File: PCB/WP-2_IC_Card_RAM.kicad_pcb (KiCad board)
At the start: 2 copper layers, 45 x 54 mm, 11 parts, among them J1 Conn_01x38_Female, U1 SRAM 128Kx8 5v Parallel, U2 SRAM 128Kx8 5v Parallel

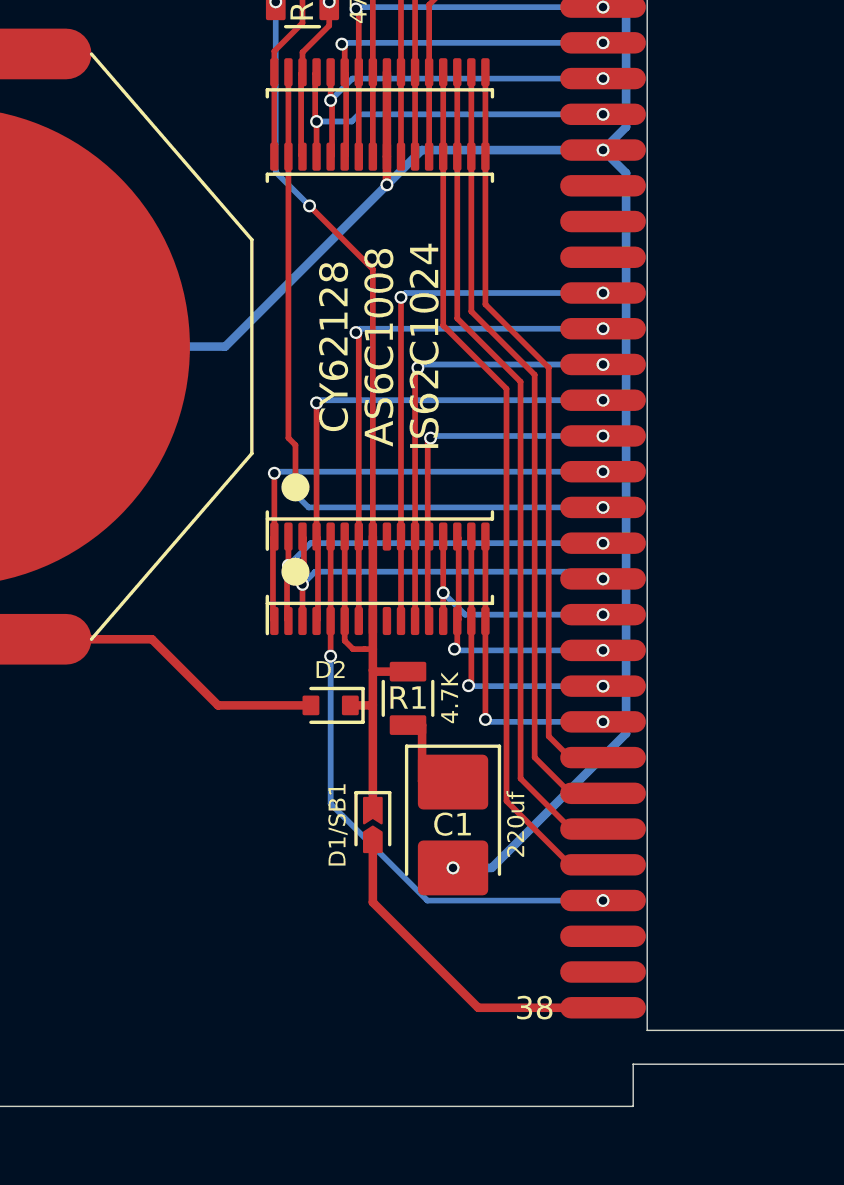
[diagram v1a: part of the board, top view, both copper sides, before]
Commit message: cap & diodes on ram card
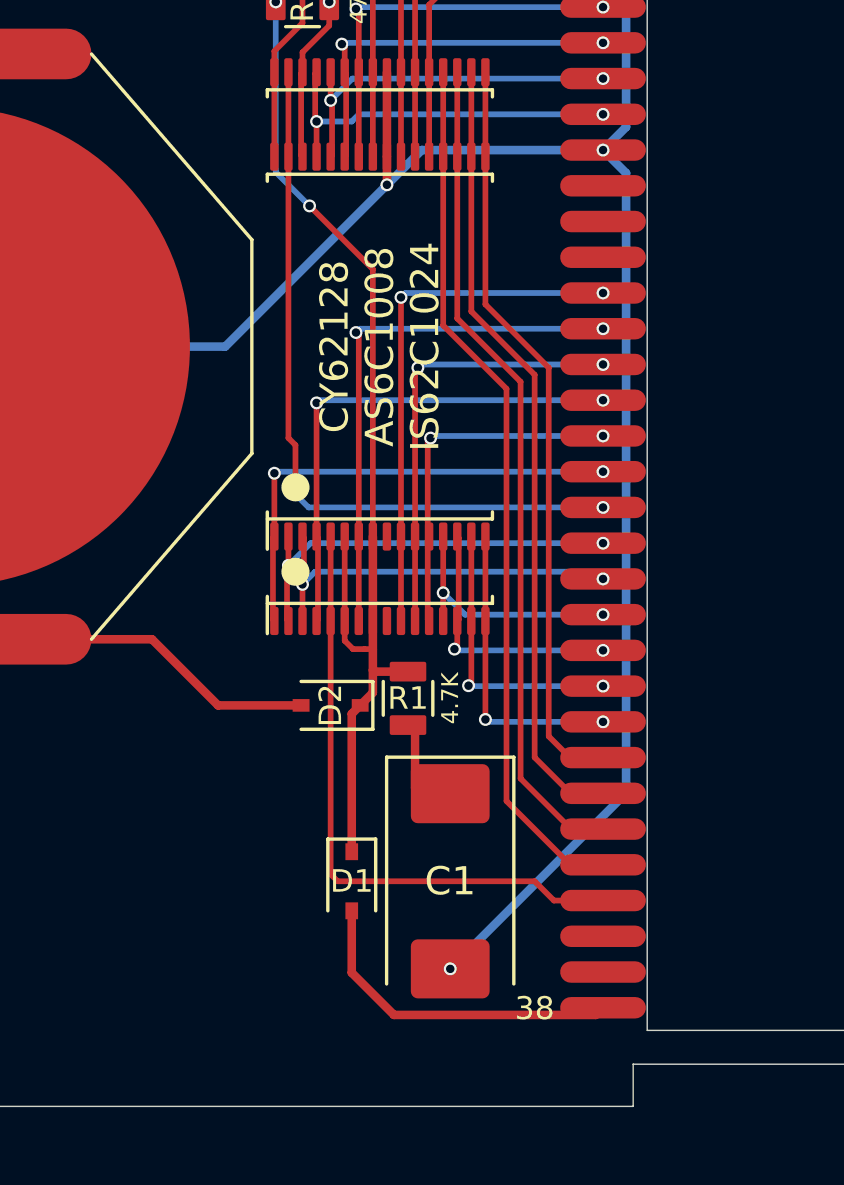
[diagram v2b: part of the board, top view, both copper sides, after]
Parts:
- C1: footprint 0_LOCAL:CP_Tantalum_Case-B_EIA-3528-21_Reflow -> 0_LOCAL:CP_EIA-7343-20_AVX-Y
- D1: renamed from D1/SB1; value 1SS389 -> CUS520,H3F; footprint 0_LOCAL:D_SOD-523_bridgeable -> 0_LOCAL:D_SOD-323
- D2: value 1SS389 -> CUS520,H3F; footprint 0_LOCAL:D_SOD-523 -> 0_LOCAL:D_SOD-323
- moved D1 2.14 mm to (148.2, 118.7)
- moved C1 2.00 mm to (151.8, 118.7)
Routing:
- net GND: track 77.0 -> 79.8 mm
- net /R~W: track 20.6 -> 22.1 mm, vias 2 -> 0
- net VMEM: track 32.3 -> 33.5 mm
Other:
- board text added: "WP-2_IC_Card_RAM_cap_batt_no_carrier v002"
- board text removed: "WP-2_IC_Card_RAM_cap_batt_no_carrier v001"

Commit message: readme
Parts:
- moved D2 0.25 mm to (147.5, 112.2)
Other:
- outline, holes or cut-outs redrawn

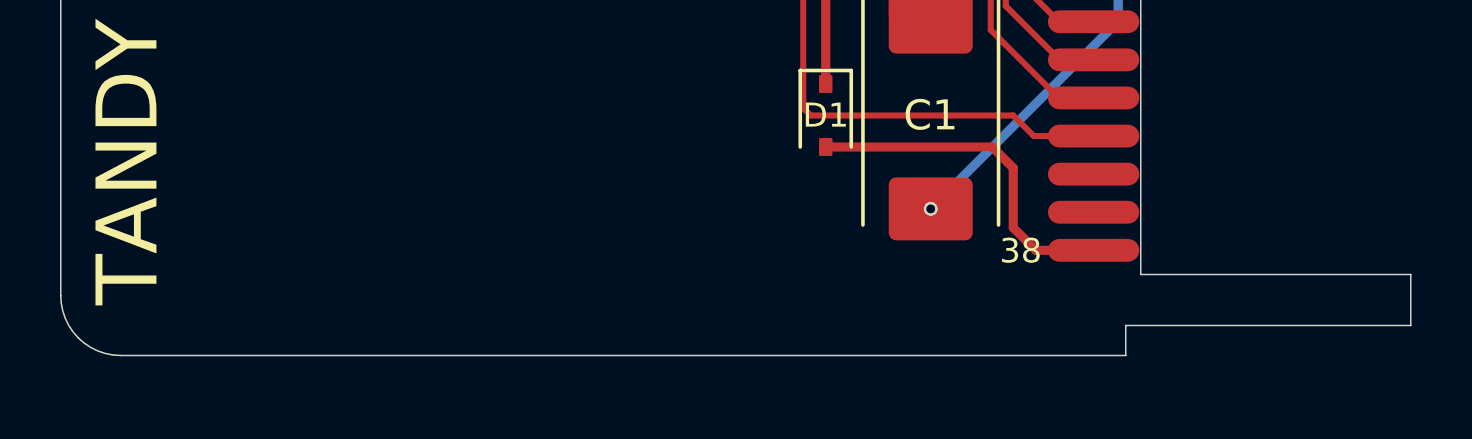
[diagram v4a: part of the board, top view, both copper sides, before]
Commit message: silkscreen board name, small board outline tweak
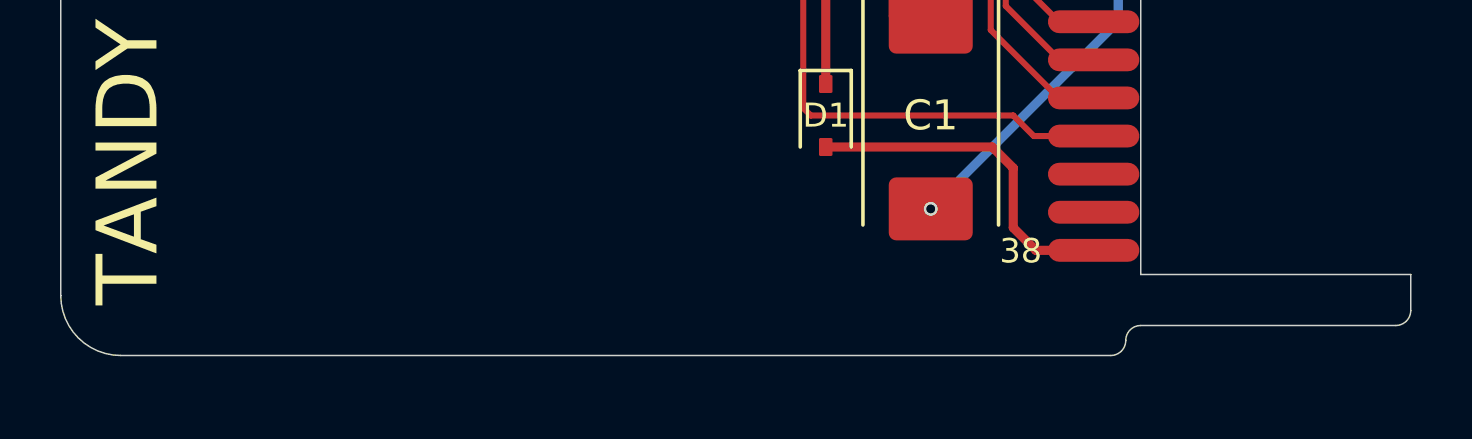
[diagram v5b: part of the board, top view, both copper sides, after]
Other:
- outline, holes or cut-outs redrawn
- board text added: "WP-2_IC_Card_RAM v002"
- board text removed: "WP-2_IC_Card_RAM_cap_batt_no_carrier v002"

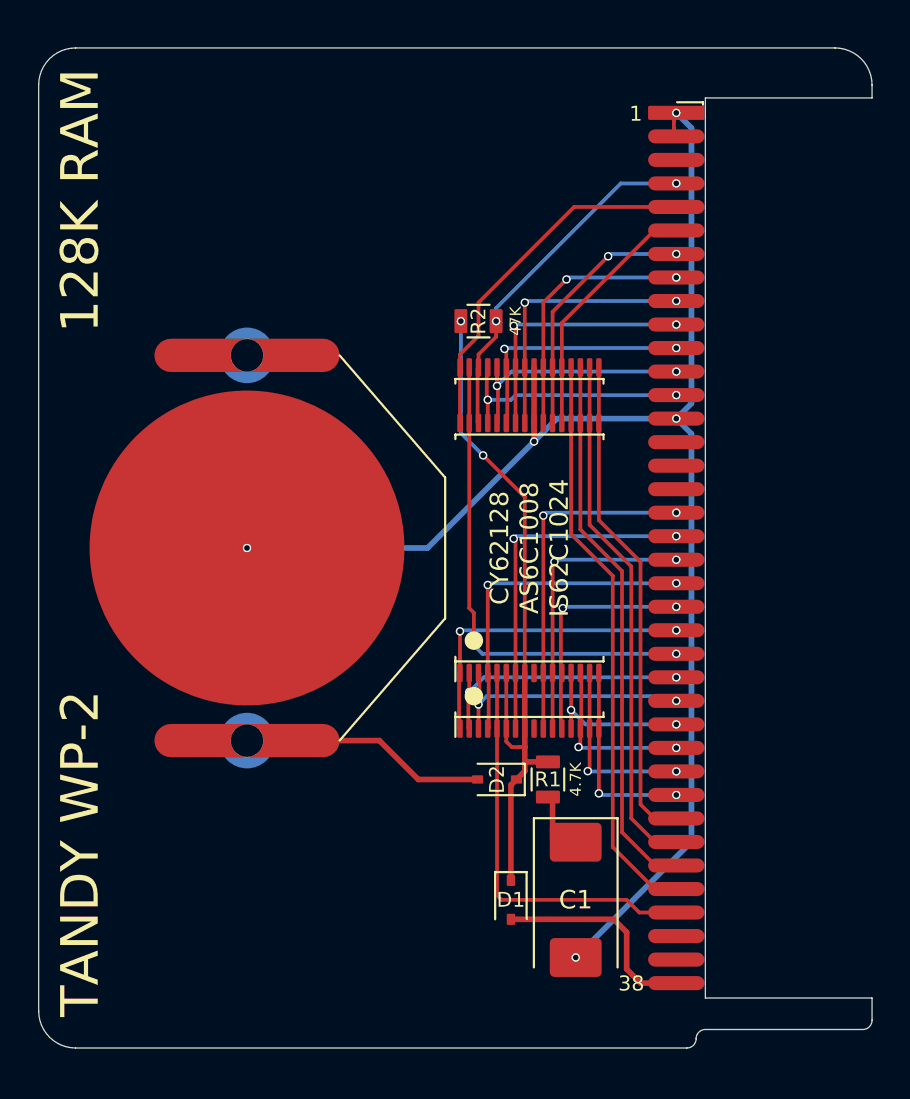
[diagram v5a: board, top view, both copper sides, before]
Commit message: v003 - edge cut finger pulls, easier diodes and batt holder for RAM
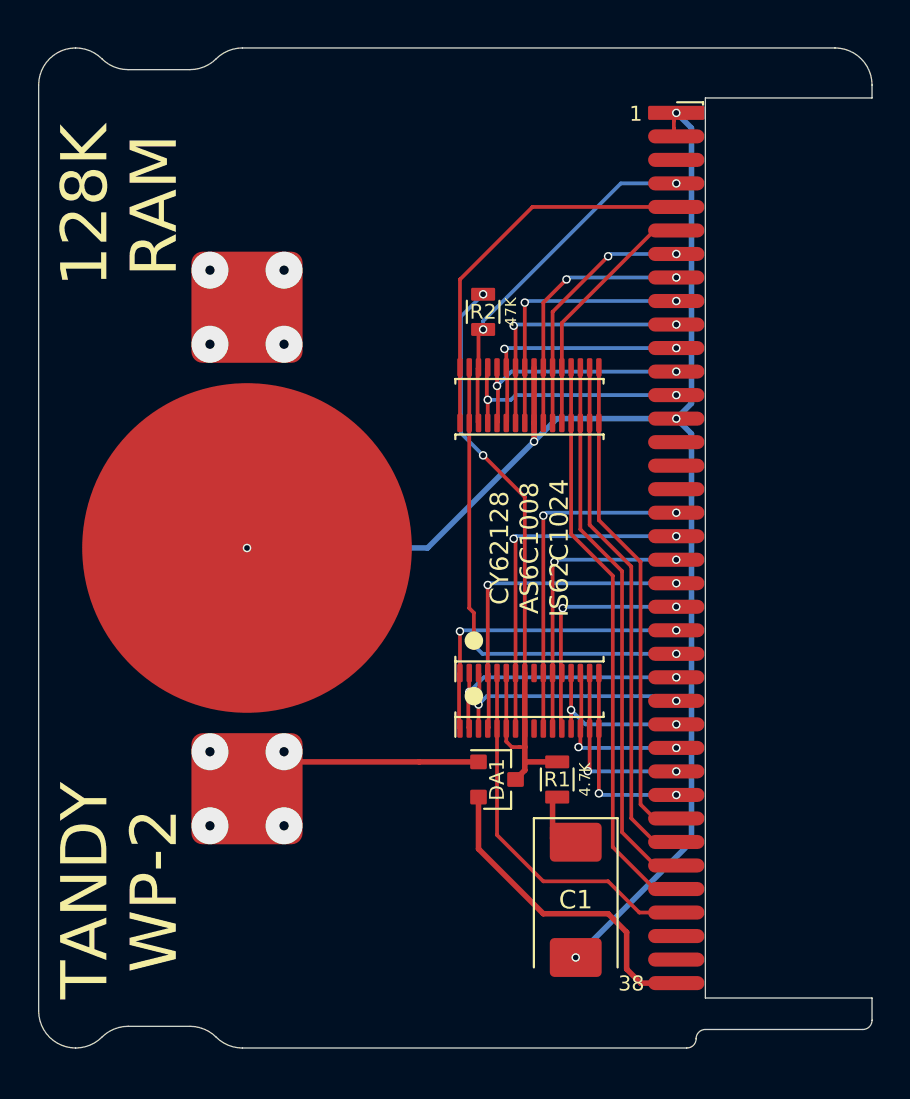
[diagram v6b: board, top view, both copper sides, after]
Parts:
- removed D1, D2: CUS520,H3F, 0_LOCAL:D_SOD-323
- added DA1: BAT54C, 0_LOCAL:SOT-23, F.Cu at (147.5, 112.2)
- BT1: value Battery CR2016 3v -> CR2016 3v; footprint 0_LOCAL:2016_battery_holder_tht -> 0_LOCAL:2016_battery_holder_smt
- moved R2 0.56 mm to (146.8, 86.9), turned to 270 degrees
- moved R1 0.50 mm to (150.8, 112.2)
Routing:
- net VBUS: track 11.5 -> 17.6 mm
- net VMEM: track 33.5 -> 30.4 mm
- net /R~W: track 22.1 -> 20.2 mm
- net /~OE: track 19.7 -> 21.1 mm
- net Net-(BT1-Pad1): track 13.3 -> 13.1 mm, vias 0 -> 8
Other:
- outline, holes or cut-outs redrawn
- board text added: "128K"
- board text added: "RAM"
- board text added: "TANDY"
- board text added: "WP-2_IC_Card_RAM v003"
- board text removed: "128K RAM"
- board text removed: "TANDY WP-2"
- board text removed: "WP-2_IC_Card_RAM v002"
